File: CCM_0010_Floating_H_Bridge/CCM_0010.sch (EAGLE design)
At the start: 60 parts, among them IC1 HIP4081A, IC2 74*1G04, Q1 TIP29, Q2 TIP30, U1 ADA4898-2, U2 AD8276, U3 BUF634, U4 AD4898-1, X1 1-227161-0, X2 22-23-2021, X3 1-227161-0, X4 22-23-2031, X5 22-23-2031, X6 22-23-2031, X7 22-23-2031

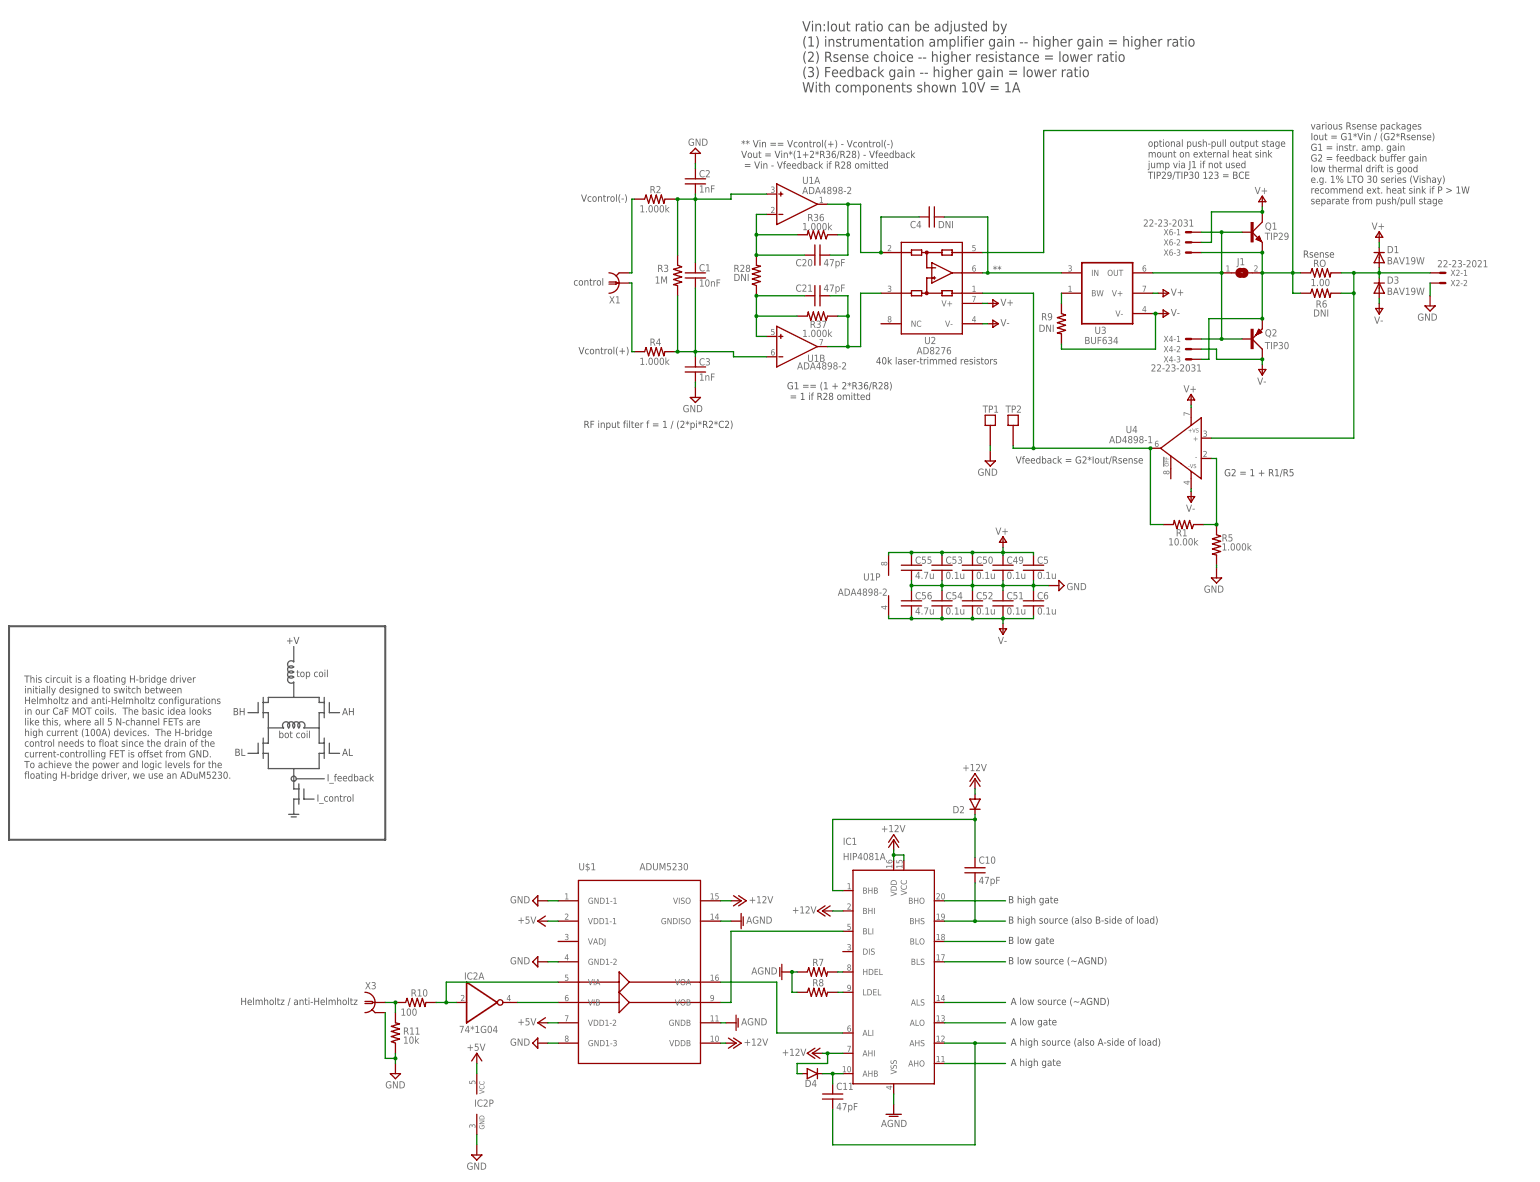
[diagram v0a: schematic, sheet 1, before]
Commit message: Added production files for CCM_0010
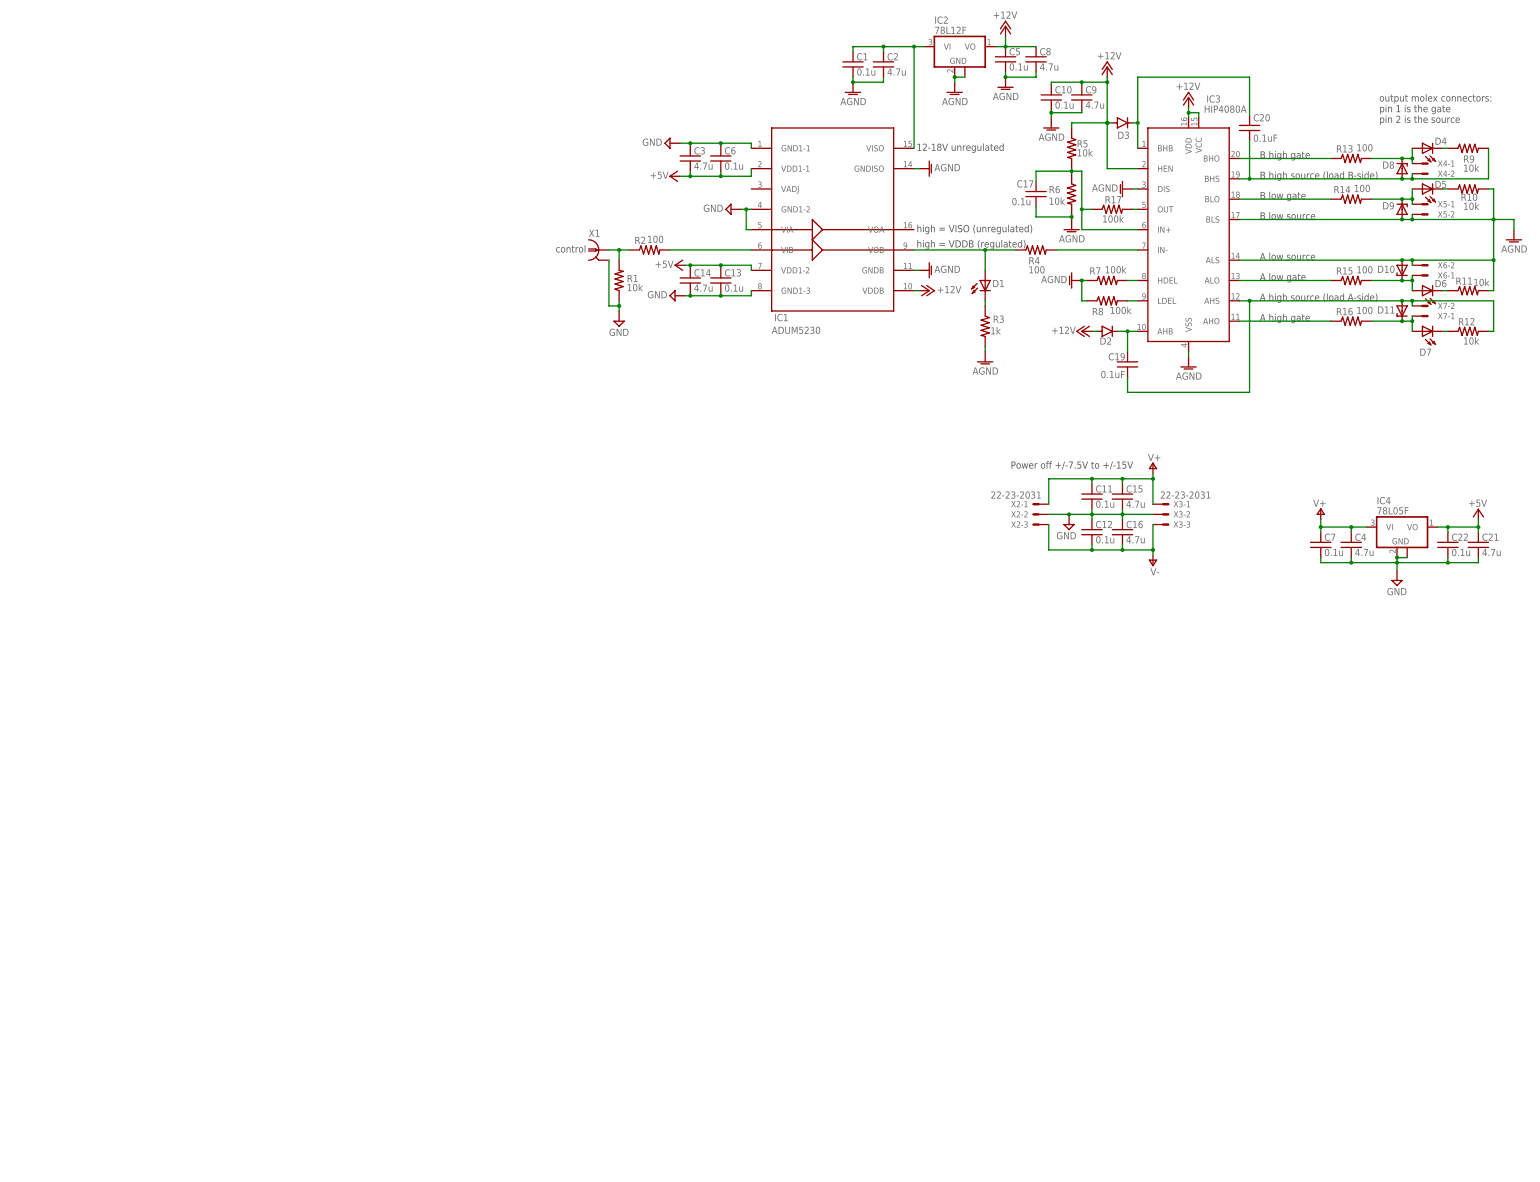
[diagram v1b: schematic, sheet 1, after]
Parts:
- removed C24, C49, C50, C51, C52, C53, C54: 0.1u, acrooptics:C0603
- removed C55, C56: 4.7u, acrooptics:C0603
- removed J1: (no value), acrooptics:SJ
- removed Q1: TIP29, transistor-power:TIP41C
- removed Q2: TIP30, transistor-power:TIP42C
- removed R28: DNI, acrooptics:R0603
- removed R36, R37: 1.000k, acrooptics:R0603
- removed RO: 1.00, noah:LT030
- removed TP1, TP2: TESTPOINT, Fitch:TESTPOINT
- removed U$1: ADUM5230, noah:ADUM5230
- removed U1: ADA4898-2, noah:ADA4898-2R
- removed U2: AD8276, noah:AD8276
- removed U3: BUF634, noah:BUF634
- removed U4: AD4898-1, noah:ADA4898-1R
- added C12, C13, C17, C22: 0.1u, acrooptics:C0603
- added C14, C15, C16: 4.7u, acrooptics:C0603
- added C19: 0.1uF, acrooptics:C0603
- added D10, D11, D8, D9: (no value), WCSMain:ZENER-DIODESOT23
- added D5, D6, D7: (no value), acrooptics:LED0603
- added IC3: HIP4080A, noah:HIP4080A
- added IC4: 78L05F, linear:78L12F
- added R12: 10k, acrooptics:R0603
- added R13, R14, R15, R16: 100, acrooptics:R0603
- added R17: 100k, acrooptics:R0603
- C1: value 10nF -> 0.1u
- C10, C11: value 47pF -> 0.1u
- C2, C3: value 1nF -> 4.7u
- C20: value 47pF -> 0.1uF
- C21: value 47pF -> 4.7u
- C4: value DNI -> 4.7u
- C7: value 4.7u -> 0.1u
- C8: value 0.1u -> 4.7u
- D1: value BAV19W -> (none); device AquariumLibrary:DIODE-SOD123 -> acrooptics:LED0603
- D3: value BAV19W -> (none); device AquariumLibrary:DIODE-SOD123 -> WCSMain:DIODESOT23
- D4: device WCSMain:DIODESOT23 -> acrooptics:LED0603
- IC1: value HIP4081A -> ADUM5230; device noah:HIP4081A -> noah:ADUM5230
- IC2: value 74*1G04 -> 78L12F; device noah:74AHC1G04DBV -> linear:78L12F
- R1: value 10.00k -> 10k
- R10: value 100 -> 10k
- R2, R4: value 1.000k -> 100
- R3: value 1M -> 1k
- R5: value 1.000k -> 10k
- R6: value DNI -> 10k; device noah:RESISTOR2512 -> acrooptics:R0603
- R7, R8: value (none) -> 100k
- R9: value DNI -> 10k
- X2: value 22-23-2021 -> 22-23-2031; device con-molex:22-23-2021 -> con-molex:22-23-2031
- X3: value 1-227161-0 -> 22-23-2031; device con-coax:1-227161-0 -> con-molex:22-23-2031
- X4, X5, X6, X7: value 22-23-2031 -> 22-23-2021; device con-molex:22-23-2031 -> con-molex:22-23-2021
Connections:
- removed net N$14: R9.1, U3.BW
- removed net N$15: R1.2, TP2.P$1, U2.REF, U4.OUT
- removed net N$26: C20.1, R28.2, R36.2, U1A.IN-
- removed net N$27: IC1.ALS
- removed net N$31: C21.1, R28.1, R37.2, U1B.IN+
- removed net N$33: C21.2, R37.1, U1B.OUT, U2.+IN
- removed net N$35: C20.2, C4.1, R36.1, U1A.OUT, U2.-IN
- new net N$24: IC3.HDEL, R7.2
- net +12V: now also C10.1, C5.1, C8.1, C9.1, D3.A, IC1.VDDB, IC2.VO, IC3.HEN, IC3.VCC, IC3.VDD, R5.1; no longer D4.A, IC1.AHI, IC1.BHI, IC1.VCC, IC1.VDD, U$1.VDDB, U$1.VISO
- net +5V: now also C13.1, C14.1, C21.1, C22.1, C3.2, C6.2, IC1.VDD1-1, IC1.VDD1-2, IC4.VO; no longer IC2P.VCC, U$1.VDD1-1, U$1.VDD1-2
- net AGND: now also C1.2, C10.2, C17.2, C2.2, C5.2, C8.2, C9.2, D10.A, D9.A, IC1.GNDB, IC1.GNDISO, IC2.GND, IC2.GND@1, IC3.ALS, IC3.BLS, IC3.DIS, IC3.VSS, R10.2, R11.2, R3.2, R6.2, X5-2.S, X6-2.S; no longer IC1.VSS, U$1.GNDB, U$1.GNDISO
- net GND: now also C11.2, C12.1, C13.2, C14.2, C15.2, C16.1, C21.2, C22.2, C3.1, C4.2, IC1.GND1-1, IC1.GND1-2, IC1.GND1-3, IC1.VIA, IC4.GND, IC4.GND@1, R1.1, X1.2, X3-2.S; no longer C2.1, C24.1, C3.2, C49.2, C5.2, C50.2, C51.1, C52.1, C53.2, C54.1, C55.2, C56.1, C8.2, C9.1, IC2P.GND, R11.1, R5.2, TP1.P$1, U$1.GND1-1, U$1.GND1-2, U$1.GND1-3, X3.2, X5-2.S, X7-2.S
- net N$1: now also D1.C, R3.1; no longer R2.1, X1.2
- net N$10: now also C1.1, C2.1, IC1.VISO, IC2.VI; no longer IC2A.I, R10.2, U$1.VIA
- net N$11: now also IC3.AHO, R16.1; no longer D1.A, D3.C, R6.2, RO.2, U4.IN+, X2-1.S
- net N$12: now also IC3.ALO, R15.1; no longer J1.2, Q1.E, Q2.E, R6.1, RO.1, U2.SENSE, X4-3.S, X6-3.S
- net N$13: now also IC3.IN-, R4.2; no longer IC1.ALI, U$1.VOA
- net N$16: now also IC3.LDEL, R8.2; no longer IC1.BLI, U$1.VOB
- net N$17: now also C20.2, D3.C, IC3.BHB; no longer C10.2, D2.C, IC1.BHB
- net N$18: now also C20.1, D8.A, IC3.BHS, R9.2, X4-2.S; no longer C10.1, IC1.BHS
- net N$19: now also IC3.BLO, R14.1; no longer IC1.BLO
- net N$2: now also D4.C, R9.1; no longer R4.1, X1.1
- net N$20: now also IC3.OUT, R17.2; no longer IC1.BLS
- net N$21: now also C19.1, D11.A, IC3.AHS, R12.2, X7-2.S; no longer C11.1, IC1.AHS
- net N$22: now also D11.C, D7.A, R16.2, X7-1.S; no longer IC1.AHO
- net N$23: now also C19.2, D2.C, IC3.AHB; no longer C11.2, D4.C, IC1.AHB
- net N$25: now also D10.C, D6.A, R15.2, X6-1.S; no longer IC1.ALO
- net N$28: now also R1.2, R2.1, X1.1; no longer R10.1, R11.2, X3.1
- net N$29: now also C17.1, IC3.IN+, R17.1, R5.2, R6.1; no longer IC1.HDEL, R7.2
- net N$3: now also D5.C, R10.1; no longer C4.2, U2.OUT, U3.IN
- net N$30: now also IC1.VIB, R2.2; no longer IC1.LDEL, R8.2
- net N$4: now also IC3.BHO, R13.1; no longer IC1.BHO
- net N$5: now also D5.A, D9.C, R14.2, X5-1.S; no longer C1.1, C2.2, R2.2, R3.1, U1A.IN+
- net N$6: now also D6.C, R11.1; no longer C1.2, C3.1, R3.2, R4.2, U1B.IN-
- net N$7: now also D4.A, D8.C, R13.2, X4-1.S; no longer R1.1, R5.1, U4.IN-
- net N$8: now also D1.A, IC1.VOB, R4.1; no longer IC2A.O, U$1.VIB
- net N$9: now also D7.C, R12.1; no longer J1.1, Q1.B, Q2.B, U3.OUT, X4-1.S, X6-1.S
- net V+: now also C11.1, C15.1, C4.1, IC4.VI, X2-1.S, X3-1.S; no longer C49.1, C5.1, C50.1, C53.1, C55.1, C8.1, D1.C, Q1.C, U1P.V+, U2.V+, U3.V+, U4.+VS, X5-1.S, X6-2.S, X7-1.S
- net V-: now also C12.2, C16.2, X2-3.S, X3-3.S; no longer C24.2, C51.2, C52.2, C54.2, C56.2, C6.2, C9.2, D3.A, Q2.C, R9.2, U1P.V-, U2.V-, U3.V-, U4.-VS, X4-2.S, X5-3.S, X7-3.S
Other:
- note added: "12-18V unregulated"
- note added: "A full configuration using 2 of this circuit uses 9 FETs and 2 logic signals to give 4 possibilities: (1) anti-Helmholtz direction 1 (2) anti-Helmholtz direction 2 (3) Helmholtz direction 1 (4) Helmholtz direction 2"
- note added: "A high source (load A-side)"
- note added: "A low source"
- note added: "B high source (load B-side)"
- note added: "B low source"
- note added: "CH"
- note added: "CL"
- note added: "DH"
- note added: "DL"
- note added: "Power off +/-7.5V to +/-15V"
- note added: "This circuit is a floating H-bridge driver initially designed to switch between Helmholtz and anti-Helmholtz configurations in our CaF MOT coils. The power/output stage looks like this, where all 5 N-channel FETs are high current (100A) devices. The H-bridge control needs to float since the drain of the current-controlling FET is offset from GND. To float the power and logic levels for the H-brid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"
- note added: "Using a slightly different configuration, this circuit can be used to easily reverse the both MOT coil currents simultaneously as you might like to do if you want to switch between a red-detuned and blue-detuned MOT and/or molasses. In this configuration the body diodes do the protection for you, there is no need for an external one."
- note added: "high = VDDB (regulated)"
- note added: "high = VISO (unregulated)"
- note added: "output molex connectors: pin 1 is the gate pin 2 is the source"
- note removed: "**"
- note removed: "** Vin == Vcontrol(+) - Vcontrol(-) Vout = Vin*(1+2*R36/R28) - Vfeedback = Vin - Vfeedback if R28 omitted"
- note removed: "40k laser-trimmed resistors"
- note removed: "A high source (also A-side of load)"
- note removed: "A low source (~AGND)"
- note removed: "B high source (also B-side of load)"
- note removed: "B low source (~AGND)"
- note removed: "G1 == (1 + 2*R36/R28) = 1 if R28 omitted"
- note removed: "G2 = 1 + R1/R5"
- note removed: "Helmholtz / anti-Helmholtz"
- note removed: "Power off +/-5V to +/-15V use lowest practical supply voltage to reduce output stage power dissipation"
- note removed: "RF input filter f = 1 / (2*pi*R2*C2)"
- note removed: "Rsense"
- note removed: "This circuit is a floating H-bridge driver initially designed to switch between Helmholtz and anti-Helmholtz configurations in our CaF MOT coils. The basic idea looks like this, where all 5 N-channel FETs are high current (100A) devices. The H-bridge control needs to float since the drain of the current-controlling FET is offset from GND. To achieve the power and logic levels for the floating H-b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"
- note removed: "Vcontrol(+)"
- note removed: "Vcontrol(-)"
- note removed: "Vfeedback = G2*Iout/Rsense"
- note removed: "Vin:Iout ratio can be adjusted by (1) instrumentation amplifier gain -- higher gain = higher ratio (2) Rsense choice -- higher resistance = lower ratio (3) Feedback gain -- higher gain = lower ratio With components shown 10V = 1A"
- note removed: "optional push-pull output stage mount on external heat sink jump via J1 if not used TIP29/TIP30 123 = BCE"
- note removed: "various Rsense packages Iout = G1*Vin / (G2*Rsense) G1 = instr. amp. gain G2 = feedback buffer gain low thermal drift is good e.g. 1% LTO 30 series (Vishay) recommend ext. heat sink if P > 1W separate from push/pull stage"
- moved on the sheet: C1, C10, C11, C2, C20, C21, C3, C4, C5, C6, D2, R1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

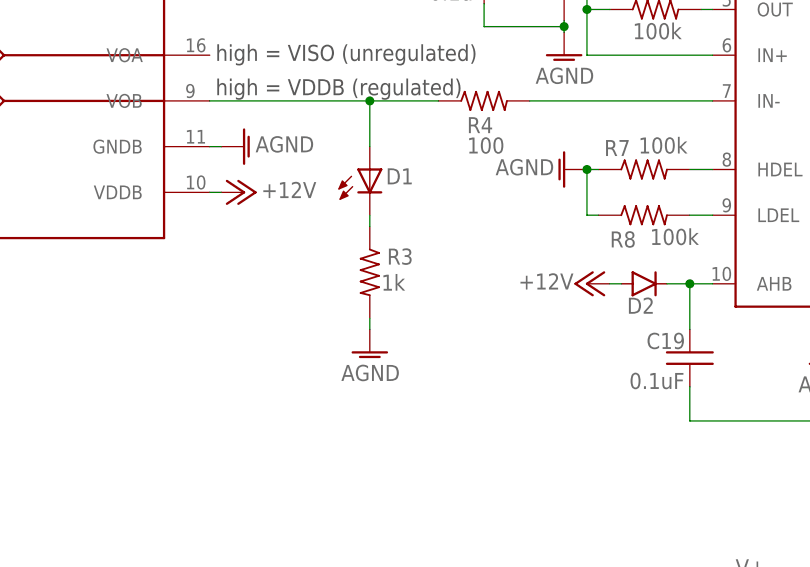
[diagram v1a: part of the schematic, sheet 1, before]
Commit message: CCM_0010: component value updates
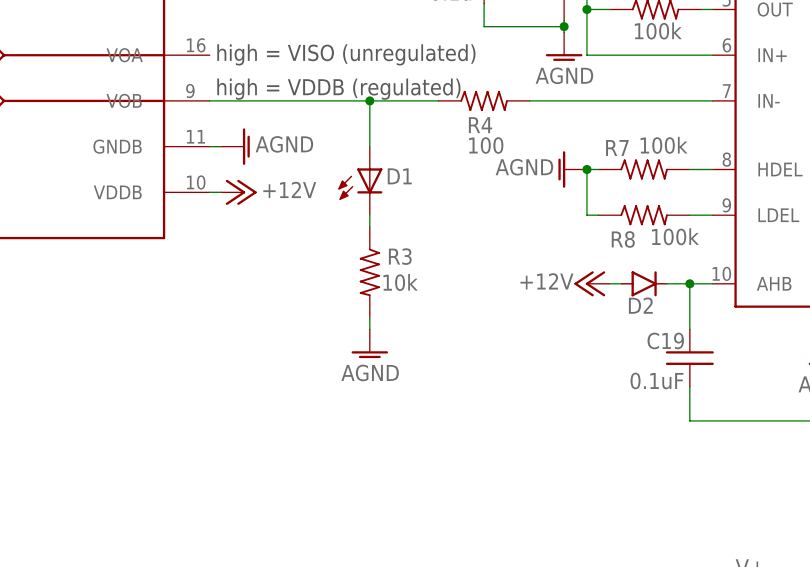
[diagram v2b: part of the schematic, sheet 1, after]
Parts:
- R3: value 1k -> 10k
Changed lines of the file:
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@@
 <part name="R4" library="acrooptics" deviceset="R" device="0603" value="100"/>
 <part name="D1" library="acrooptics" deviceset="LED" device="0603"/>
-<part name="R3" library="acrooptics" deviceset="R" device="0603" value="1k"/>
+<part name="R3" library="acrooptics" deviceset="R" device="0603" value="10k"/>
 <part name="AGND5" library="supply1" library_urn="urn:adsk.eagle:library:371" deviceset="AGND" device=""/>
 <part name="X4" library="con-molex" library_urn="urn:adsk.eagle:library:165" deviceset="22-23-2021" device=""/>

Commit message: started design of hardware TCL
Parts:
- R10, R11, R12, R3, R9: value 10k -> 51k
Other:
- note added: "A full configuration using 2 of this circuit uses 9 FETs and 2 logic signals to give 4 possibilities: (1) anti-Helmholtz direction 1 (2) anti-Helmholtz direction 2 (3) Helmholtz direction 1 (4) Helmholtz direction 2 This is the most flexible configuration and the body diodes do all the protection for you, no need for any external ones."
- note added: "Power off +/-15V"
- note removed: "A full configuration using 2 of this circuit uses 9 FETs and 2 logic signals to give 4 possibilities: (1) anti-Helmholtz direction 1 (2) anti-Helmholtz direction 2 (3) Helmholtz direction 1 (4) Helmholtz direction 2"
- note removed: "Power off +/-7.5V to +/-15V"
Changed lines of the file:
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@@
 <part name="R4" library="acrooptics" deviceset="R" device="0603" value="100"/>
 <part name="D1" library="acrooptics" deviceset="LED" device="0603"/>
-<part name="R3" library="acrooptics" deviceset="R" device="0603" value="10k"/>
+<part name="R3" library="acrooptics" deviceset="R" device="0603" value="51k"/>
 <part name="AGND5" library="supply1" library_urn="urn:adsk.eagle:library:371" deviceset="AGND" device=""/>
 <part name="X4" library="con-molex" library_urn="urn:adsk.eagle:library:165" deviceset="22-23-2021" device=""/>
 <part name="X5" library="con-molex" library_urn="urn:adsk.eagle:library:165" deviceset="22-23-2021" device=""/>
 <part name="D4" library="acrooptics" deviceset="LED" device="0603"/>
-<part name="R9" library="acrooptics" deviceset="R" device="0603" value="10k"/>
+<part name="R9" library="acrooptics" deviceset="R" device="0603" value="51k"/>
 <part name="D5" library="acrooptics" deviceset="LED" device="0603"/>
-<part name="R10" library="acrooptics" deviceset="R" device="0603" value="10k"/>
+<part name="R10" library="acrooptics" deviceset="R" device="0603" value="51k"/>
 <part name="X6" library="con-molex" library_urn="urn:adsk.eagle:library:165" deviceset="22-23-2021" device=""/>
 <part name="D6" library="acrooptics" deviceset="LED" device="0603"/>
-<part name="R11" library="acrooptics" deviceset="R" device="0603" value="10k"/>
+<part name="R11" library="acrooptics" deviceset="R" device="0603" value="51k"/>
 <part name="X7" library="con-molex" library_urn="urn:adsk.eagle:library:165" deviceset="22-23-2021" device=""/>
 <part name="D7" library="acrooptics" deviceset="LED" device="0603"/>
-<part name="R12" library="acrooptics" deviceset="R" device="0603" value="10k"/>
+<part name="R12" library="acrooptics" deviceset="R" device="0603" value="51k"/>
 <part name="D8" library="WCSMain" deviceset="ZENER-DIODE" device="SOT23"/>
 <part name="D9" library="WCSMain" deviceset="ZENER-DIODE" device="SOT23"/>
@@
 <text x="99.695" y="116.205" size="1.778" layer="97">high = VISO (unregulated)</text>
 <text x="99.695" y="112.395" size="1.778" layer="97">high = VDDB (regulated)</text>
-<text x="123.19" y="57.15" size="1.778" layer="97">Power off +/-7.5V to +/-15V</text>
+<text x="119.38" y="58.42" size="1.778" layer="97">Power off +/-15V</text>
 <text x="215.265" y="143.51" size="1.778" layer="97">output molex connectors:
 pin 1 is the gate
@@
 <text x="201.295" y="66.04" size="1.778" layer="97">bot
 coil</text>
-<text x="134.62" y="104.14" size="1.778" layer="97">A full configuration using 2 of this circuit uses 9 FETs
+<text x="127" y="93.345" size="1.778" layer="97">A full configuration using 2 of this circuit uses 9 FETs
 and 2 logic signals to give 4 possibilities:
 (1) anti-Helmholtz direction 1
 (2) anti-Helmholtz direction 2
 (3) Helmholtz direction 1
-(4) Helmholtz direction 2</text>
+(4) Helmholtz direction 2
+This is the most flexible configuration and the body
+diodes do all the protection for you, no need for any
+external ones.</text>
 <circle x="203.2" y="58.42" radius="0.635" width="0.1524" layer="97"/>
 <wire x1="203.835" y1="58.42" x2="213.36" y2="58.42" width="0.1524" layer="97"/>
 <text x="213.995" y="57.785" size="1.778" layer="97">I_feedback</text>
-<wire x1="129.54" y1="124.46" x2="228.6" y2="124.46" width="0.508" layer="97"/>
+<wire x1="124.46" y1="124.46" x2="228.6" y2="124.46" width="0.508" layer="97"/>
 <wire x1="228.6" y1="124.46" x2="228.6" y2="43.18" width="0.508" layer="97"/>
-<wire x1="228.6" y1="43.18" x2="129.54" y2="43.18" width="0.508" layer="97"/>
-<wire x1="129.54" y1="43.18" x2="129.54" y2="124.46" width="0.508" layer="97"/>
+<wire x1="228.6" y1="43.18" x2="124.46" y2="43.18" width="0.508" layer="97"/>
+<wire x1="124.46" y1="43.18" x2="124.46" y2="124.46" width="0.508" layer="97"/>
 <wire x1="196.85" y1="71.12" x2="196.85" y2="74.93" width="0.1524" layer="97"/>
 <wire x1="195.58" y1="74.93" x2="198.12" y2="74.93" width="0.1524" layer="97"/>
